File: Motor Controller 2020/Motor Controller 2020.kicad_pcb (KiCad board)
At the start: 2 copper layers, 86 x 60 mm, 37 parts, among them J1 Batt+, J2 Batt-, J3 Input, J4 Motor+, J5 Motor-, Q1 IRF1404, Q2 IRF1404, Q3 IRF1404, Q4 IRF1404, Q5 IRF1404, Q6 IRF1404, Q7 IRF1404, Q8 IRF1404, SW1 SW_DIP_x03, U1 L7805, U2 a4956, U3 Attiny4313

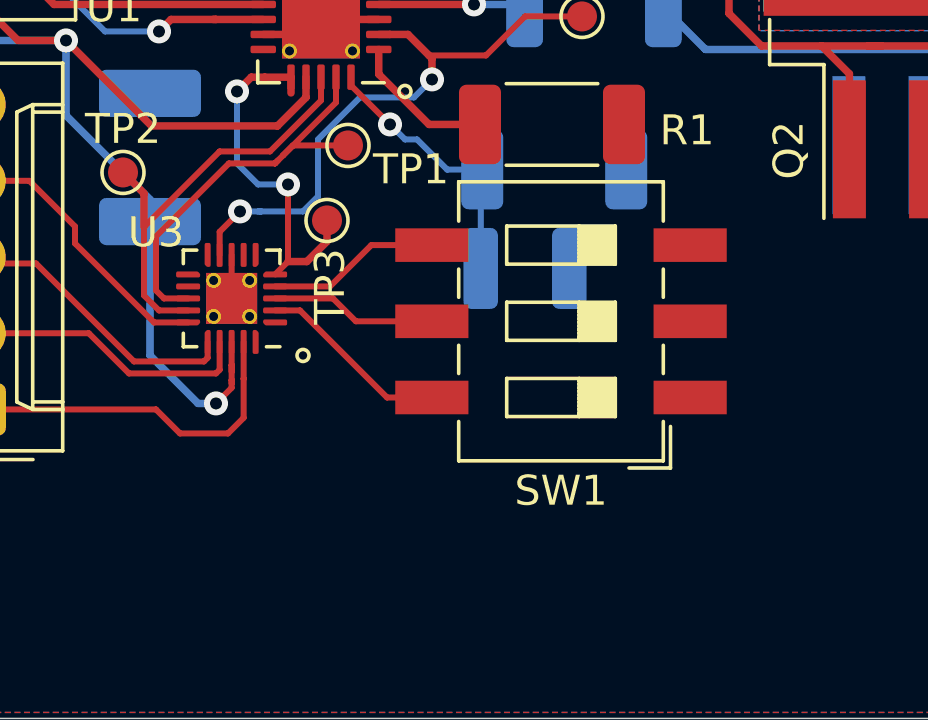
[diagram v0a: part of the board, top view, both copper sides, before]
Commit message: Added reset/program jumper to board
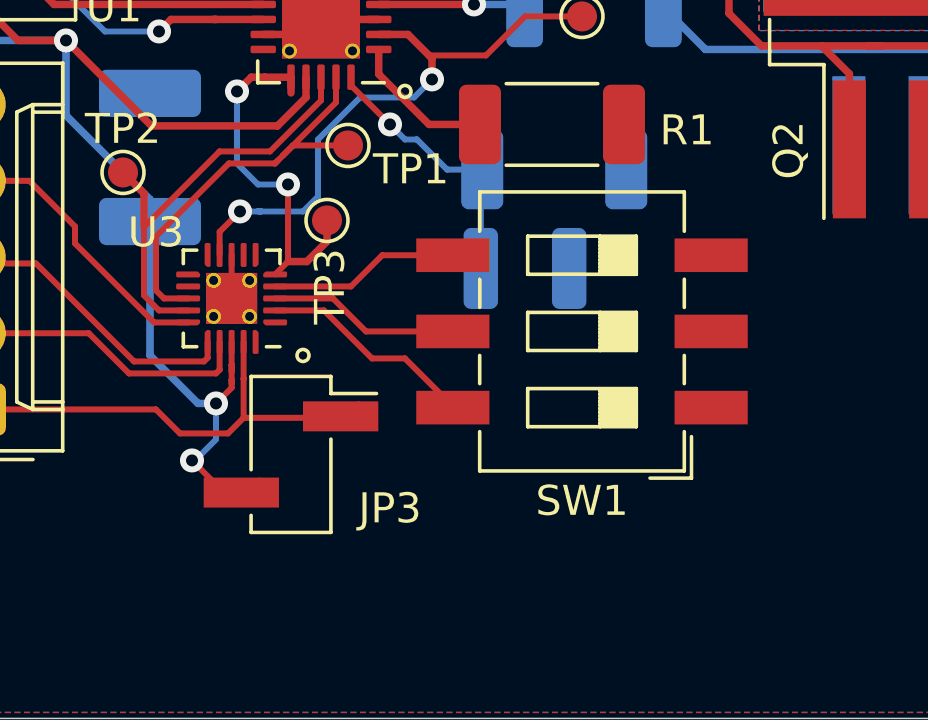
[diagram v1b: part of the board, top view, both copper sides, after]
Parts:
- added JP3: Program/Reset, Connector_PinHeader_2.54mm:PinHeader_1x02_P2.54mm_Vertical_SMD_Pin1Right, F.Cu at (119.2, 94.1)
- C6: value 600pF -> 620pF
- moved SW1 0.78 mm to (128.9, 90.0)
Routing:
- net +5V: track 38.4 -> 43.2 mm, vias 2 -> 3
- net A_RESET: track 12.1 -> 16.1 mm
- net ADDR_Select_2: track 4.59 -> 6.68 mm
- net ADDR_Select_3: track 5.48 -> 7.57 mm
- net ADDR_Select_1: track 4.85 -> 6.65 mm

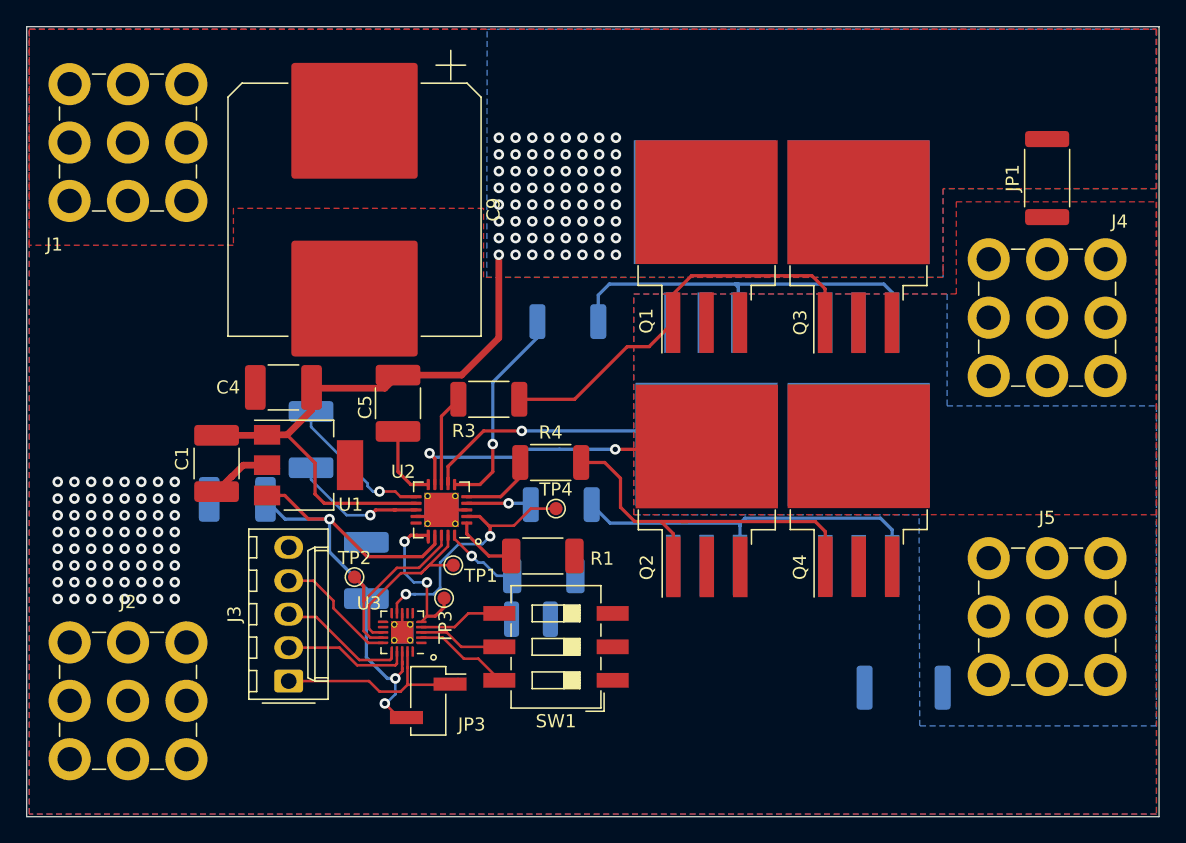
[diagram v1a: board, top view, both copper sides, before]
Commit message: Added mounting holes instead of trying to slide the board into the housing
The 3D printed slide mechanism didn't work because the printer couldn't reproduce the sharp corners
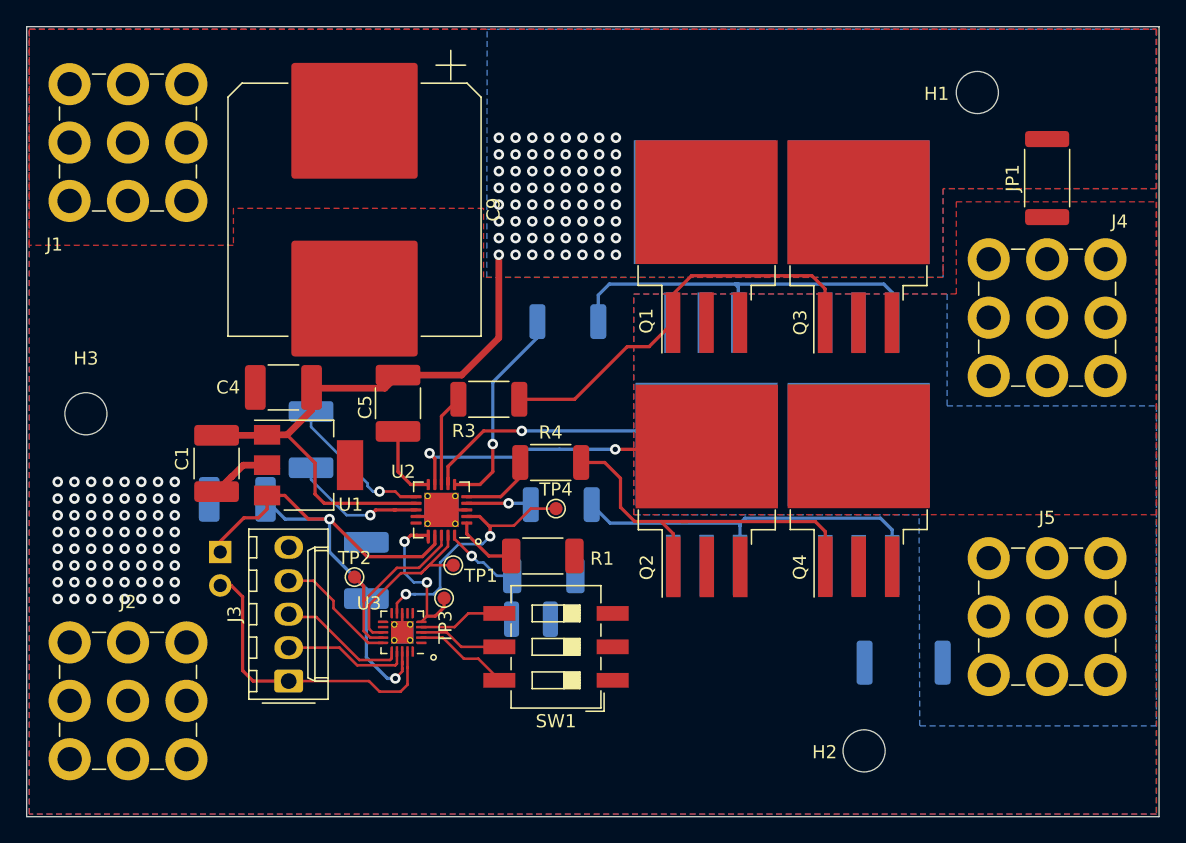
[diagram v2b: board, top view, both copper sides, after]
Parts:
- added H1: MountingHole, MountingHole:MountingHole_3.2mm_M3, F.Cu at (160.9, 47.9)
- added H2: MountingHole, MountingHole:MountingHole_3.2mm_M3, F.Cu at (152.3, 97.9)
- added H3: MountingHole, MountingHole:MountingHole_3.2mm_M3, F.Cu at (93.2, 72.3)
- JP3: footprint Connector_PinHeader_2.54mm:PinHeader_1x02_P2.54mm_Vertical_SMD_Pin1Right -> Connector_PinHeader_2.54mm:PinHeader_1x02_P2.54mm_Horizontal; moved to B.Cu
- moved JP3 19.4 mm to (103.4, 82.8), turned to 180 degrees
- moved JP2 1.90 mm to (155.3, 91.2)
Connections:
- JP3 pad 1: A_RESET -> +5V
- JP3 pad 2: +5V -> A_RESET
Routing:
- net A_RESET: track 16.1 -> 23.6 mm
- net +5V: track 43.2 -> 44.8 mm, vias 3 -> 2

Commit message: Fixed driver reset bugs
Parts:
- removed JP3: Program/Reset, Connector_PinHeader_2.54mm:PinHeader_1x02_P2.54mm_Horizontal
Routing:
- net A_RESET: track 23.6 -> 12.1 mm
- net +5V: track 44.8 -> 38.4 mm

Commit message: Tested Reset Code
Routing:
- net +5V: track 38.4 -> 40.7 mm
- net A_RESET: track 12.1 -> 10.9 mm

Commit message: Add files via upload
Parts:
- added C7: 1uF, Capacitor_SMD:C_1210_3225Metric, F.Cu at (103.5, 77.9)
- added L1: 47uH, Inductor_SMD:L_1210_3225Metric, F.Cu at (112.2, 76.9)
- C1: value 0.33uF -> 1uF; footprint Capacitor_SMD:C_1812_4532Metric_Pad1.57x3.40mm_HandSolder -> Capacitor_SMD:C_1210_3225Metric
- C2: value 0.1uF -> 10uF; footprint Capacitor_SMD:C_1812_4532Metric_Pad1.57x3.40mm_HandSolder -> Capacitor_SMD:C_1210_3225Metric
- U1: value L7805 -> MAX15062A; footprint Package_TO_SOT_SMD:SOT-223 -> Package_DFN_QFN:DFN-8_2x2mm_P0.5mm
- moved C3 3.03 mm to (113.2, 73.4), turned to 0 degrees
- moved U1 2.87 mm to (107.5, 77.4)
- moved C1 2.74 mm to (104.8, 73.9), turned to 180 degrees
- moved C2 2.58 mm to (106.8, 77.3), turned to 90 degrees
- moved R3 1.60 mm to (125.4, 71.2)
- moved C11 0.40 mm to (114.1, 84.2)
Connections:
- U1 pad 2: GND -> +12V
- U1 pad 3: +5V -> Net-(C7-Pad1)
- U1 pad 4: (no net) -> +5V
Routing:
- net +12V: track 46.4 -> 75.8 mm
- net Net-(C3-Pad2): track 11.5 -> 6.75 mm
- net Net-(L1-Pad1): track 0.00 -> 4.65 mm
- net +5V: track 40.7 -> 36.8 mm, vias 2 -> 3
- net GND: track 10.9 -> 7.10 mm, vias 64 -> 65
- net Net-(C7-Pad1): track 0.00 -> 3.56 mm
- net MOTOR+: track 26.9 -> 28.6 mm
- net Net-(Q1-Pad1): track 29.2 -> 27.6 mm
- net Fault: track 12.4 -> 13.8 mm
- net Net-(C5-Pad2): track 5.77 -> 4.99 mm
- net GHA: track 7.01 -> 7.67 mm

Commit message: Add files via upload
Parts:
- Q1, Q2, Q3, Q4, Q5, Q6, Q7, Q8: footprint Package_TO_SOT_SMD:TO-263-3_TabPin2 -> Package_TO_SOT_SMD:TO-263-2

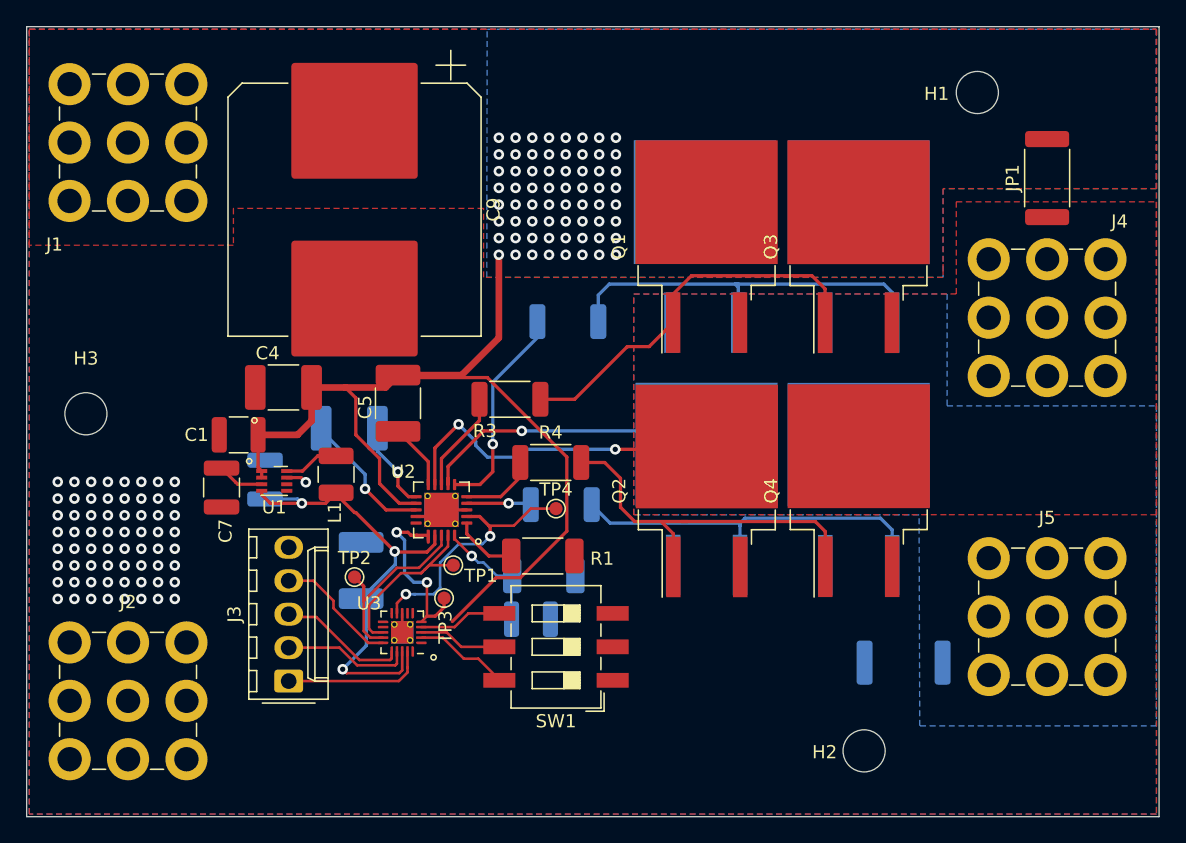
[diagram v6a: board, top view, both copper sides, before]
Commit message: Updated controller PCB
Added several capacitors to help with switching transients
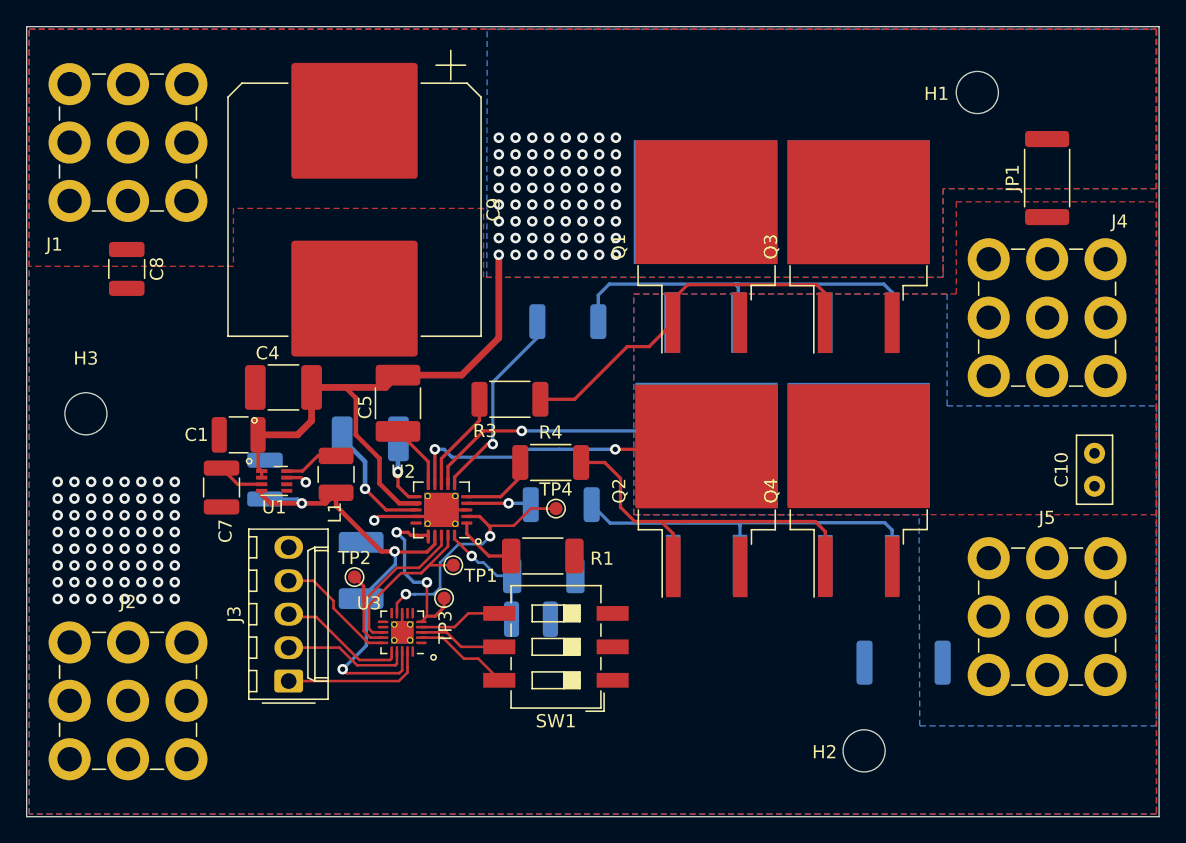
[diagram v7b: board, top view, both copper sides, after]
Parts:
- added C10: 1uF, Capacitor_THT:C_Disc_D5.0mm_W2.5mm_P2.50mm, F.Cu at (169.8, 77.8)
- added C8: 10uF, Capacitor_SMD:C_1210_3225Metric, F.Cu at (96.3, 61.3)
- moved C3 1.79 mm to (114.8, 74.2)
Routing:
- net +12V: track 75.8 -> 44.9 mm
- net GND: track 7.10 -> 10.4 mm, vias 65 -> 66
- net MOTOR+: track 28.6 -> 26.9 mm
- net Net-(C3-Pad1): track 10.7 -> 9.20 mm
- net Net-(C3-Pad2): track 6.75 -> 5.32 mm
- net Net-(Q1-Pad1): track 27.6 -> 28.8 mm
- net GHB: track 16.1 -> 15.2 mm
- net +5V: track 36.8 -> 37.6 mm

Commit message: Updated Controller board
Separated the logic and power GNDs to minimize noise. Added more Vias for current capability. Rerouted MOSFET tracks to be nearly the same length. Filleted the corners on copper pours. Added more test points for diagnosis.
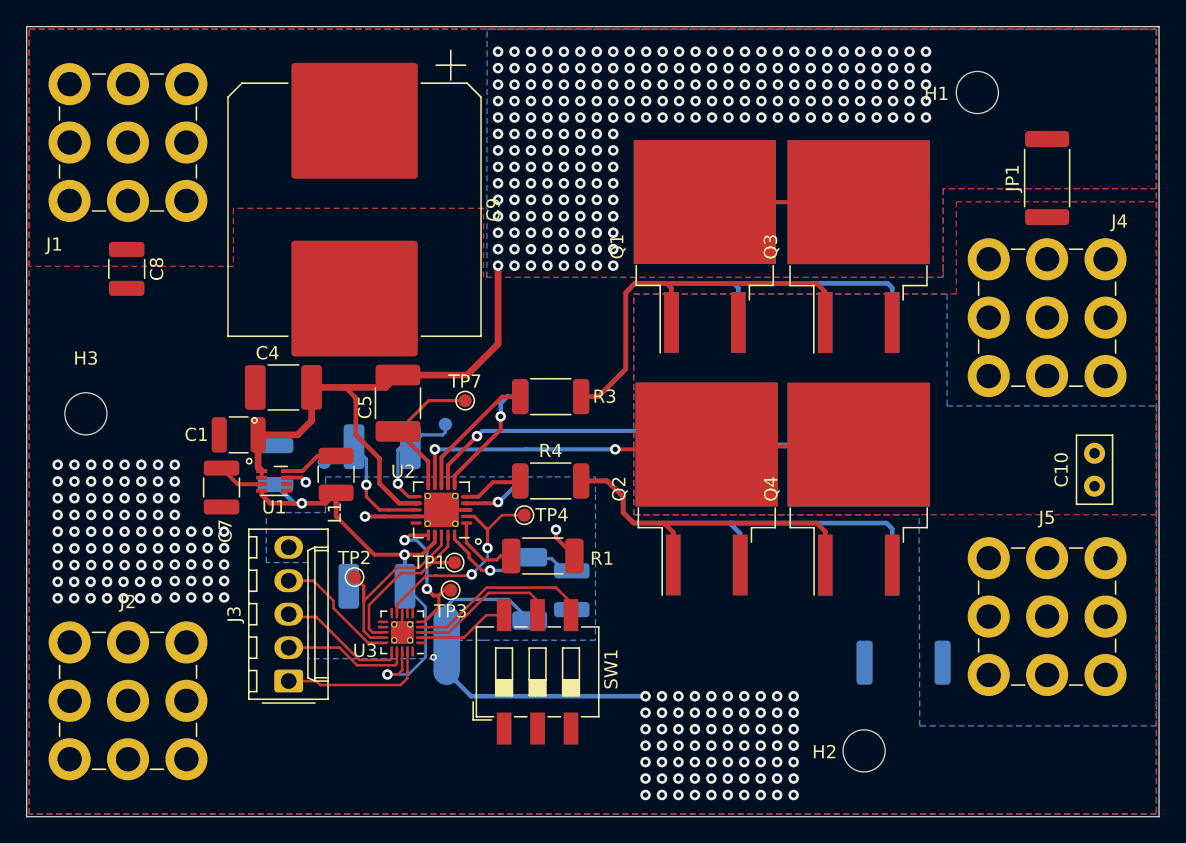
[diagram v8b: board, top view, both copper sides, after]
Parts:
- added NT1: Net-Tie_2, NetTie:NetTie-2_SMD_Pad2.0mm, B.Cu at (120.6, 89.9)
- added TP5: TestPoint, TestPoint:TestPoint_Pad_D1.0mm, B.Cu at (120.5, 73.1)
- added TP6: TestPoint, TestPoint:TestPoint_Pad_D1.0mm, B.Cu at (111.3, 76.0)
- added TP7: TestPoint, TestPoint:TestPoint_Pad_D1.0mm, F.Cu at (122.0, 71.3)
- moved R5 5.85 mm to (128.5, 71.0)
- moved C6 3.80 mm to (130.1, 85.7), turned to 270 degrees
- moved R3 3.11 mm to (128.5, 71.0)
- moved TP4 2.45 mm to (126.5, 80.0)
- moved SW1 2.36 mm to (127.5, 91.9), turned to 90 degrees
- moved R6 1.97 mm to (128.5, 77.4)
- moved C11 1.70 mm to (115.3, 85.4), turned to 0 degrees
- moved R2 1.46 mm to (126.9, 85.6), turned to 90 degrees
- moved R4 1.40 mm to (128.5, 77.4)
- moved C2 1.36 mm to (107.6, 76.2)
- moved C3 1.08 mm to (115.7, 74.8)
- moved TP3 0.78 mm to (120.9, 85.7)
- moved TP1 0.22 mm to (121.2, 83.6)
- moved Q2 0.16 mm to (140.4, 78.0)
- moved Q4 0.14 mm to (151.9, 78.0)
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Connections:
- C11 pad 1: GND -> GNDD
- C6 pad 2: GND -> GNDD
- J3 pad 5: GND -> GNDD
- R1 pad 1: GND -> GNDD
- R2 pad 1: GND -> GNDD
- U2 pad 14: GND -> GNDD
- U2 pad 21: GND -> GNDD
- U2 pad 3: GND -> GNDD
- U3 pad 21: GND -> GNDD
- U3 pad 8: GND -> GNDD
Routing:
- net +12V: track 44.9 -> 67.5 mm, vias 64 -> 207
- net GNDD: track 0.00 -> 21.0 mm, vias 0 -> 2
- net MOTOR+: track 26.9 -> 47.7 mm
- net MOTOR-: track 25.7 -> 37.7 mm
- net Net-(Q5-Pad1): track 29.9 -> 40.0 mm
- net ADDR_Select_1: track 6.65 -> 14.0 mm
- net GND: track 10.4 -> 17.5 mm, vias 66 -> 158
- net Net-(C5-Pad2): track 4.99 -> 11.3 mm
- net Net-(Q6-Pad1): track 30.5 -> 36.5 mm
- net GHB: track 15.2 -> 9.59 mm
- net ADDR_Select_2: track 6.68 -> 11.7 mm
- net Net-(C3-Pad2): track 5.32 -> 9.73 mm
- net Net-(Q1-Pad1): track 28.8 -> 33.1 mm
- net Mode: track 19.8 -> 16.6 mm
- net GHA: track 7.67 -> 10.2 mm
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- added copper zone on B.Cu, net GNDD
